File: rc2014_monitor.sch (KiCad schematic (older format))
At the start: 31 parts, among them J1 RC2014Pro, J3 USB_B_Micro, SW1 SW_Coded_Octal-8, U1 74HCT138, U2 74HCT151, U3 74HCT244, U4 74HCT244, U5 74HCT244, U6 74HCT32, U7 MAX40200AUK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

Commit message: added additional LED for 5V signal
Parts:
- removed RN1: R_Network06, Resistor_THT:R_Array_SIP7, symbol Device:R_Network06
- added LED6: SMD Red 620nm 40mcd 2.2V; 20mA, LED_SMD:LED_0805_2012Metric_Pad1.15x1.40mm_HandSolder, symbol Device:LED_Small
- added RN1: 270R Bussed, Resistor_THT:R_Array_SIP9, symbol Device:R_Network08
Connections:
- wire segments 151 -> 158
- no-connect marks 28 -> 26
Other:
- note added: "5V"
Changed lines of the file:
@@
-$EndComp
-$Comp
-L Device:R_Network06 RN1
-U 1 1 5CBFD2C7
-P 4850 3850
-F 0 "RN1" V 4333 3850 50  0000 C CNN
-F 1 "R_Network06" V 4424 3850 50  0000 C CNN
-F 2 "Resistor_THT:R_Array_SIP7" V 5225 3850 50  0001 C CNN
-F 3 "https://www.mouser.com/datasheet/2/54/600x-776645.pdf" H 4850 3850 50  0001 C CNN
-F 4 "652-4607X-1LF-270" V 4850 3850 50  0001 C CNN "MouserPN"
-F 5 "Bourns" H -500 50  50  0001 C CNN "MFR"
-F 6 "4607X-101-271LF" H -500 50  50  0001 C CNN "MPN"
-F 7 "Mouser" H -500 50  50  0001 C CNN "SPR"
-F 8 "652-4607X-1LF-270" H -500 50  50  0001 C CNN "SPN"
-F 9 "-" H -500 50  50  0001 C CNN "SPURL"
-	1    4850 3850
-	0    1    1    0
 $EndComp
 $Comp
@@
 NoConn ~ 1000 7000
 NoConn ~ 1000 7100
-NoConn ~ 4000 4250
-NoConn ~ 4000 4150
-NoConn ~ 4000 4050
 NoConn ~ 2550 1650
 NoConn ~ 2550 1750
@@
 NoConn ~ 10350 1650
 NoConn ~ 10350 1750
-NoConn ~ 4650 4050
 NoConn ~ 1000 6700
 NoConn ~ 1000 6800
@@
 Wire Wire Line
 	5550 6850 5750 6850
+$Comp
+L Device:R_Network08 RN1
+U 1 1 5CAEF515
+P 4850 3950
+F 0 "RN1" V 4233 3950 50  0000 C CNN
+F 1 "270R Bussed" V 4324 3950 50  0000 C CNN
+F 2 "Resistor_THT:R_Array_SIP9" V 5325 3950 50  0001 C CNN
+F 3 "https://www.mouser.com/datasheet/2/54/600x-776645.pdf" H 4850 3950 50  0001 C CNN
+F 4 "Bourns" V 4850 3950 50  0001 C CNN "MFR"
+F 5 "4609X-101-271LF" V 4850 3950 50  0001 C CNN "MPN"
+F 6 "Mouser" V 4850 3950 50  0001 C CNN "SPR"
+F 7 "652-4609X-1LF-270" V 4850 3950 50  0001 C CNN "SPN"
+F 8 "https://www.mouser.com/ProductDetail/652-4609X-1LF-270" V 4850 3950 50  0001 C CNN "SPURL"
+	1    4850 3950
+	0    1    1    0
+$EndComp
+NoConn ~ 4650 4150
+NoConn ~ 4650 4250
+$Comp
+L Device:LED_Small LED6
+U 1 1 5CB2ECC4
+P 4350 4050
+AR Path="/5CB2ECC4" Ref="LED6"  Part="1"
+AR Path="/5CB63856/5CB2ECC4" Ref="LED?"  Part="1"
+AR Path="/5CB5AB00/5CB63856/5CB2ECC4" Ref="LED?"  Part="1"
+F 0 "LED6" H 4500 4100 50  0000 C CNN
+F 1 "SMD Red 620nm 40mcd 2.2V; 20mA" H 4250 4100 50  0001 C CNN
+F 2 "LED_SMD:LED_0805_2012Metric_Pad1.15x1.40mm_HandSolder" V 4350 4050 50  0001 C CNN
+F 3 "https://www.mouser.com/datasheet/2/348/sml-h1(c)-e-1508182.pdf" V 4350 4050 50  0001 C CNN
+F 4 "755-SML-H12U8TT86C" H -500 150 50  0001 C CNN "MouserPN"
+F 5 "ROHM Semiconductor" H -500 150 50  0001 C CNN "MFR"
+F 6 "SML-H12U8TT86C" H -500 150 50  0001 C CNN "MPN"
+F 7 "Mouser" H -500 150 50  0001 C CNN "SPR"
+F 8 "755-SML-H12U8TT86C" H -500 150 50  0001 C CNN "SPN"
+F 9 "-" H -500 150 50  0001 C CNN "SPURL"
+	1    4350 4050
+	1    0    0    -1
+$EndComp
+Wire Wire Line
+	4450 4050 4650 4050
+Wire Wire Line
+	4250 4050 4050 4050
+Text Notes 4050 4050 0    50   ~ 0
+5V
+Wire Wire Line
+	4000 4150 4050 4150
+Wire Wire Line
+	4050 4150 4050 4050
+Connection ~ 4050 4050
+Wire Wire Line
+	4050 4050 4000 4050
+Wire Wire Line
+	4000 4250 4050 4250
+Wire Wire Line
+	4050 4250 4050 4150
+Connection ~ 4050 4150
 $EndSCHEMATC

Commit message: Added mounting hole
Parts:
- SW1: footprint Button_Switch_THT:Nidec_Copal_SH-7010C -> Button_Switch_THT:SW_Greyhill_94HBB08RAT_Octal_Angled
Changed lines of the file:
@@
 F 0 "SW1" H 2325 5317 50  0000 C CNN
 F 1 "SW_Coded_Octal-8" H 2325 5226 50  0000 C CNN
-F 2 "Button_Switch_THT:Nidec_Copal_SH-7010C" H 2275 4975 50  0001 C CNN
+F 2 "Button_Switch_THT:SW_Greyhill_94HBB08RAT_Octal_Angled" H 2275 4975 50  0001 C CNN
 F 3 "https://www.mouser.com/datasheet/2/626/DIP_Series_94H-334494.pdf" H 2275 4975 50  0001 C CNN
 F 4 "706-94HBB08RAT" H 2450 4450 50  0001 C CNN "Mouser PN"

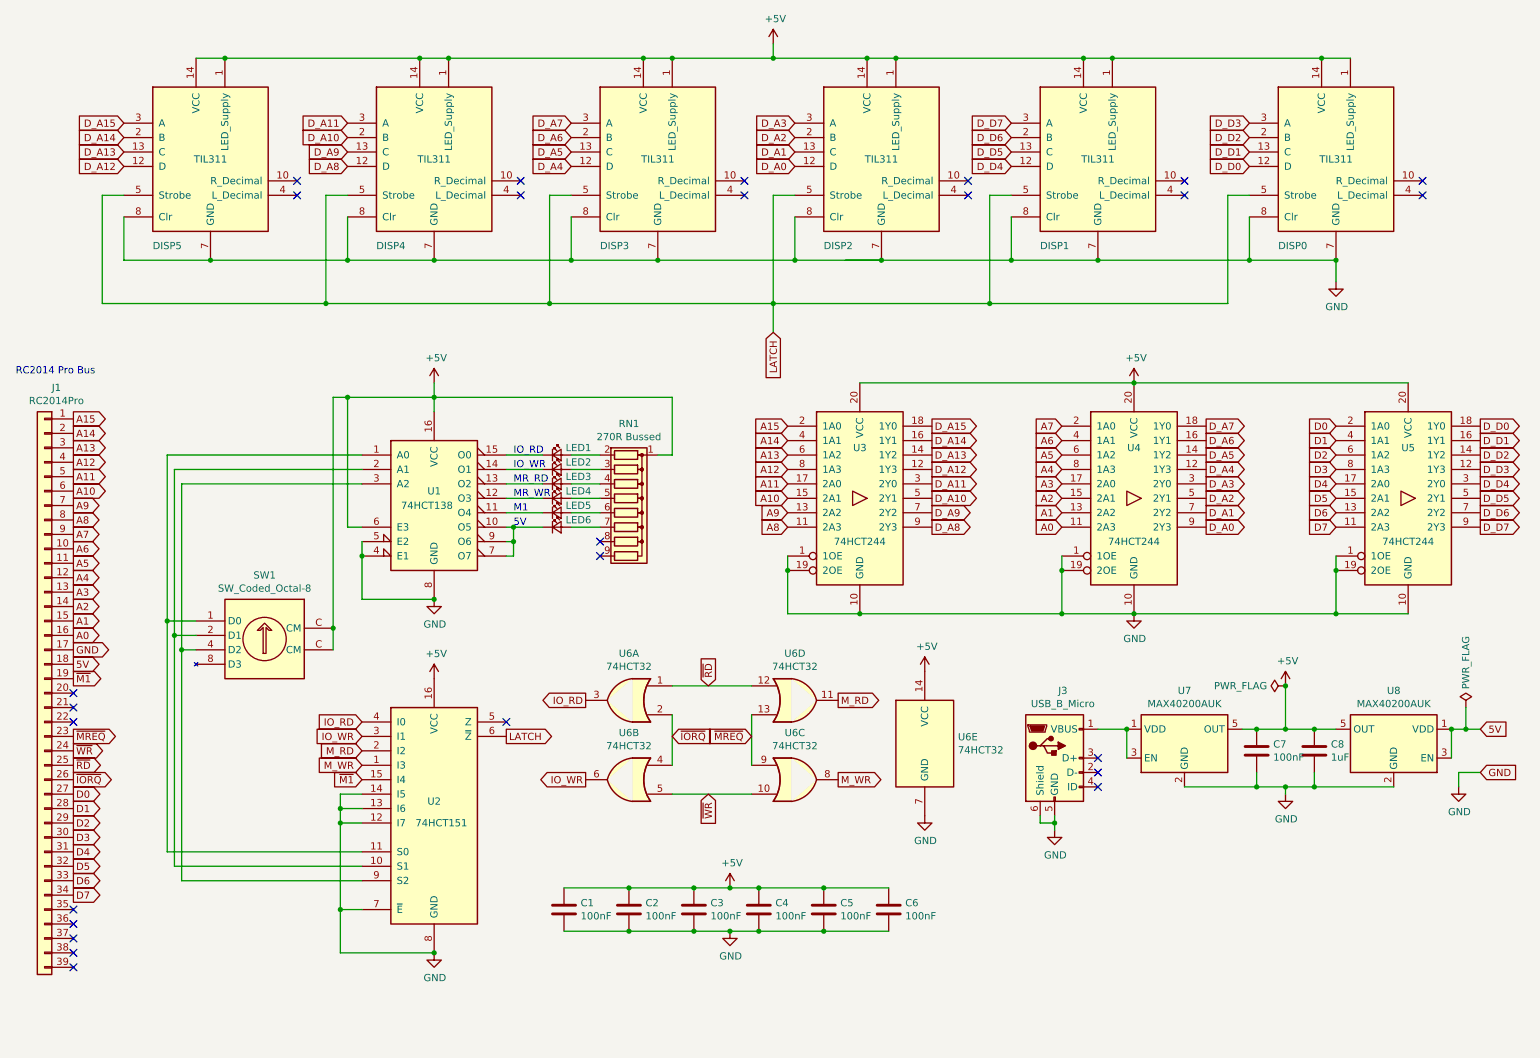
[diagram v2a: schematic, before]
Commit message: moved latch circuit to new sheet
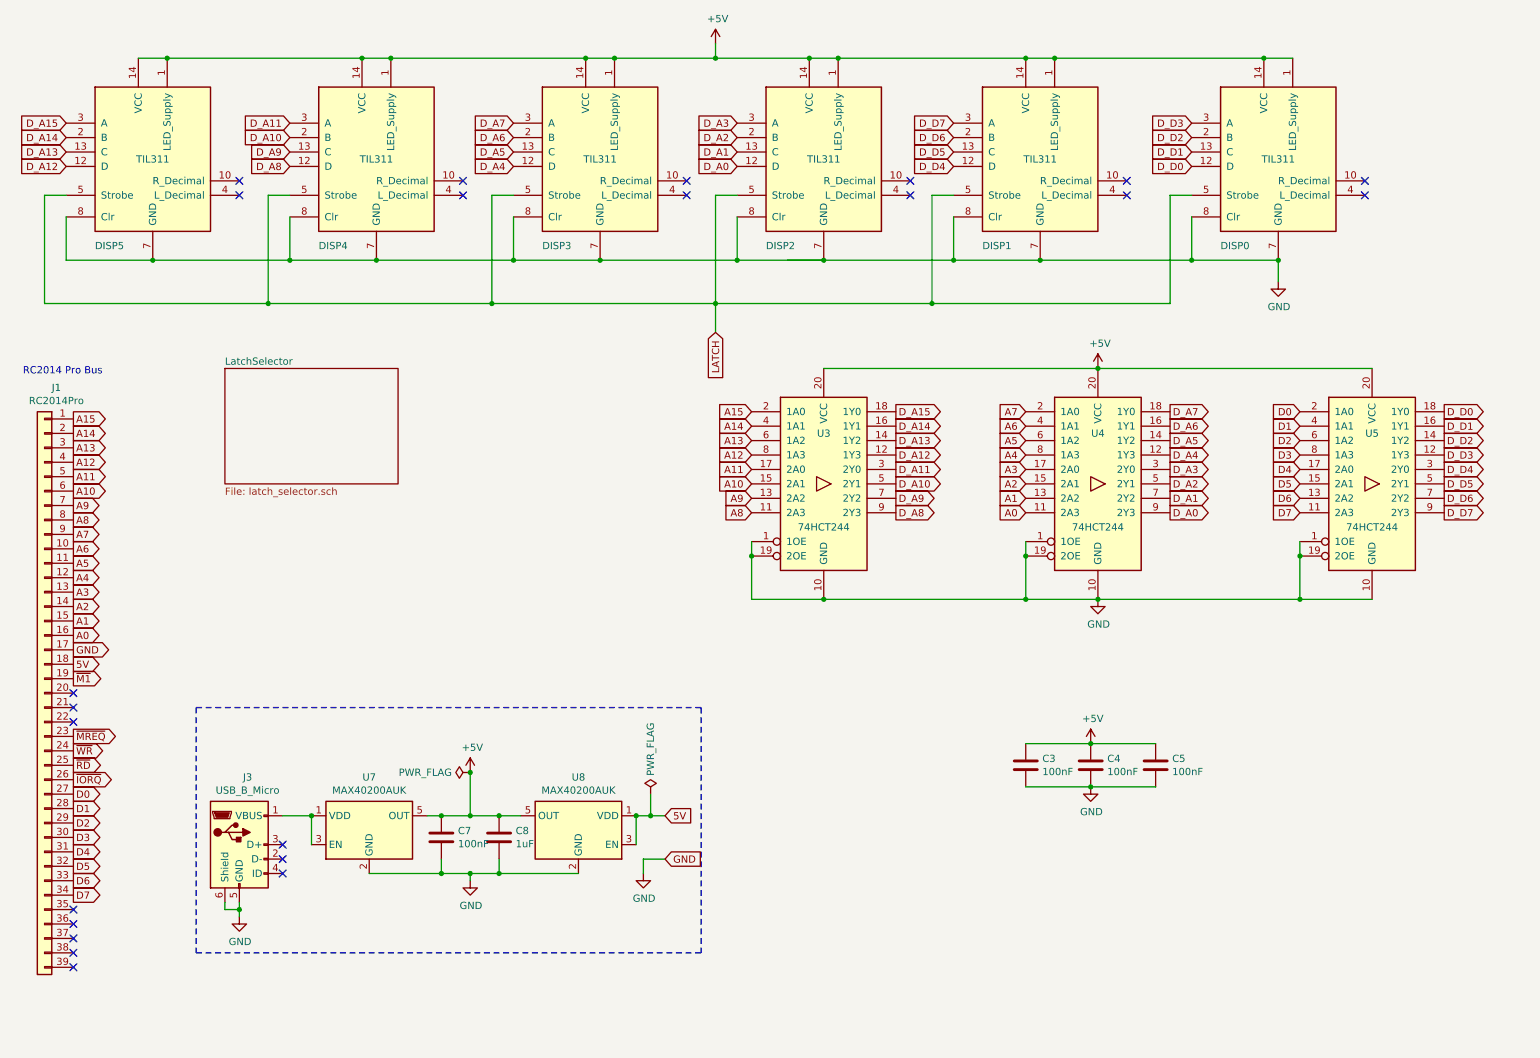
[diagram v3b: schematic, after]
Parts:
- removed C1, C2, C6: 100nF, Capacitor_THT:C_Disc_D5.0mm_W2.5mm_P2.50mm, symbol Device:C
- removed LED1, LED2, LED3, LED4, LED5, LED6: SMD Red 620nm 40mcd 2.2V; 20mA, LED_SMD:LED_0805_2012Metric_Pad1.15x1.40mm_HandSolder, symbol Device:LED_Small
- removed RN1: 270R Bussed, Resistor_THT:R_Array_SIP9, symbol Device:R_Network08
- removed SW1: SW_Coded_Octal-8, Button_Switch_THT:SW_Greyhill_94HBB08RAT_Octal_Angled, symbol rc2014_monitor-rescue:SW_Coded_Octal-8-Switch
- removed U1: 74HCT138, Package_DIP:DIP-16_W7.62mm, symbol rc2014_monitor-rescue:74HCT138-74xx
- removed U2: 74HCT151, Package_DIP:DIP-16_W7.62mm, symbol rc2014_monitor-rescue:74HCT151-74xx
- removed U6: 74HCT32, Package_DIP:DIP-14_W7.62mm, symbol rc2014_monitor-rescue:74HCT32-74xx
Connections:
- no-connect marks 26 -> 23
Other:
- note removed: "5V"
- note removed: "IO_RD\n"
- note removed: "IO_WR"
- note removed: "M1"
- note removed: "MR_RD"
- note removed: "MR_WR"
- moved on the sheet: C3, C4, C5, C7, C8, DISP0, DISP1, DISP2, DISP3, DISP4, DISP5, J3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

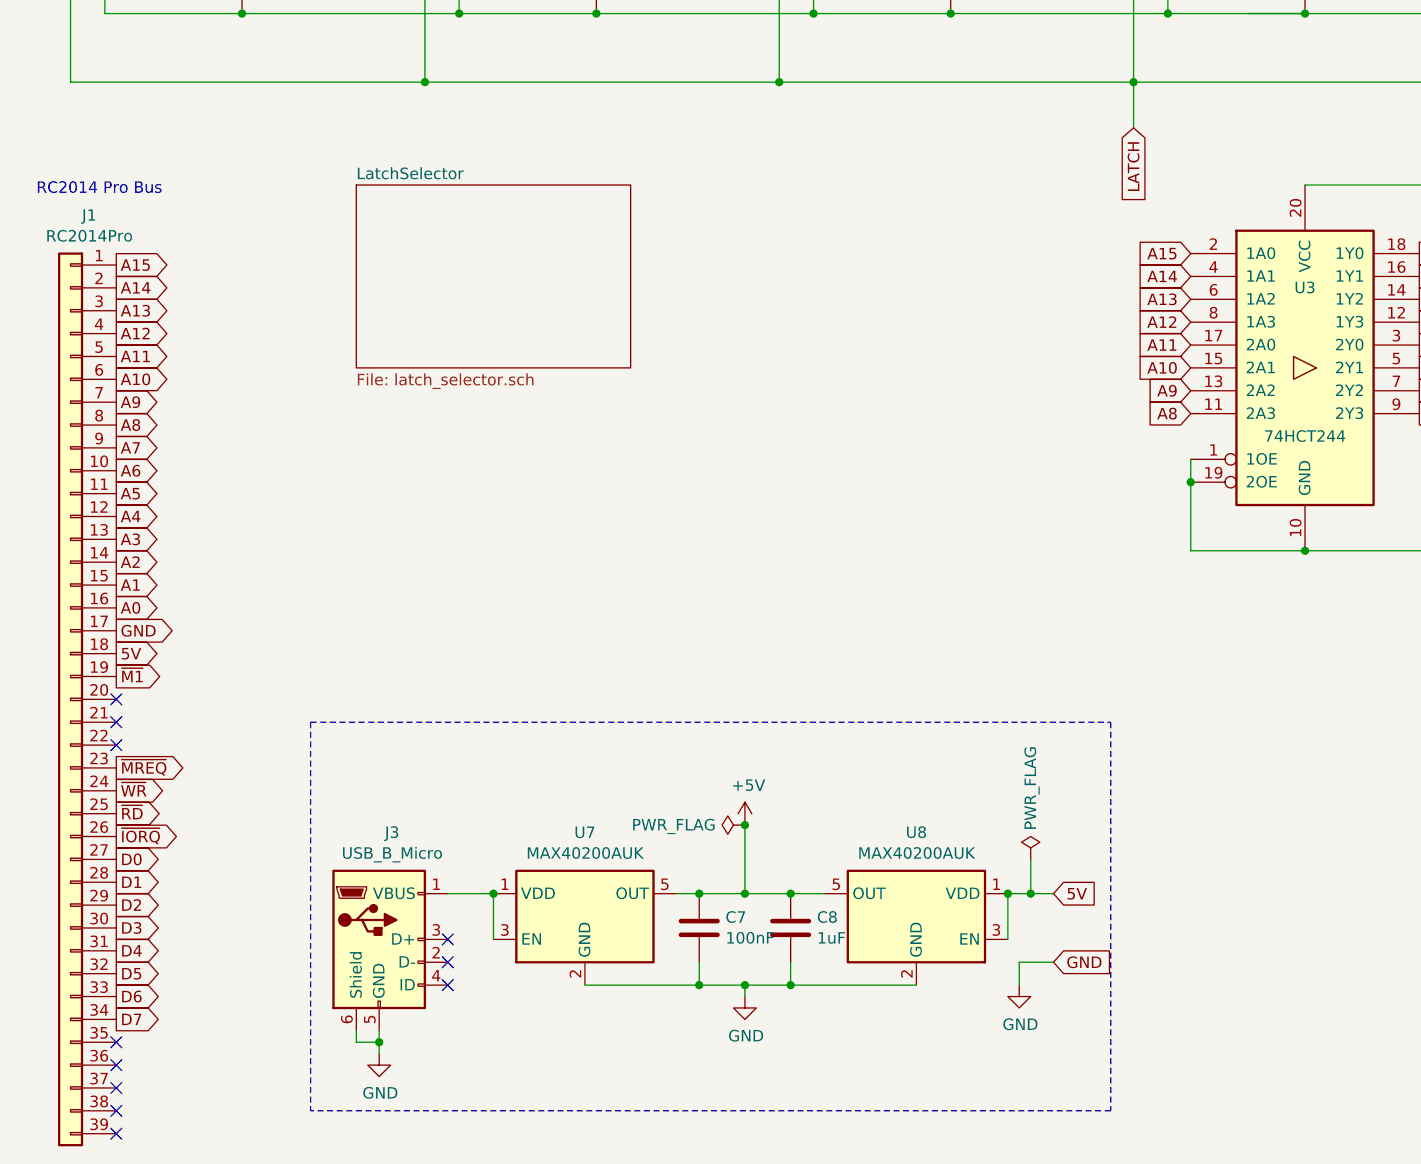
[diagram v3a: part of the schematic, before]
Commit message: added pro bus, generated gerbers
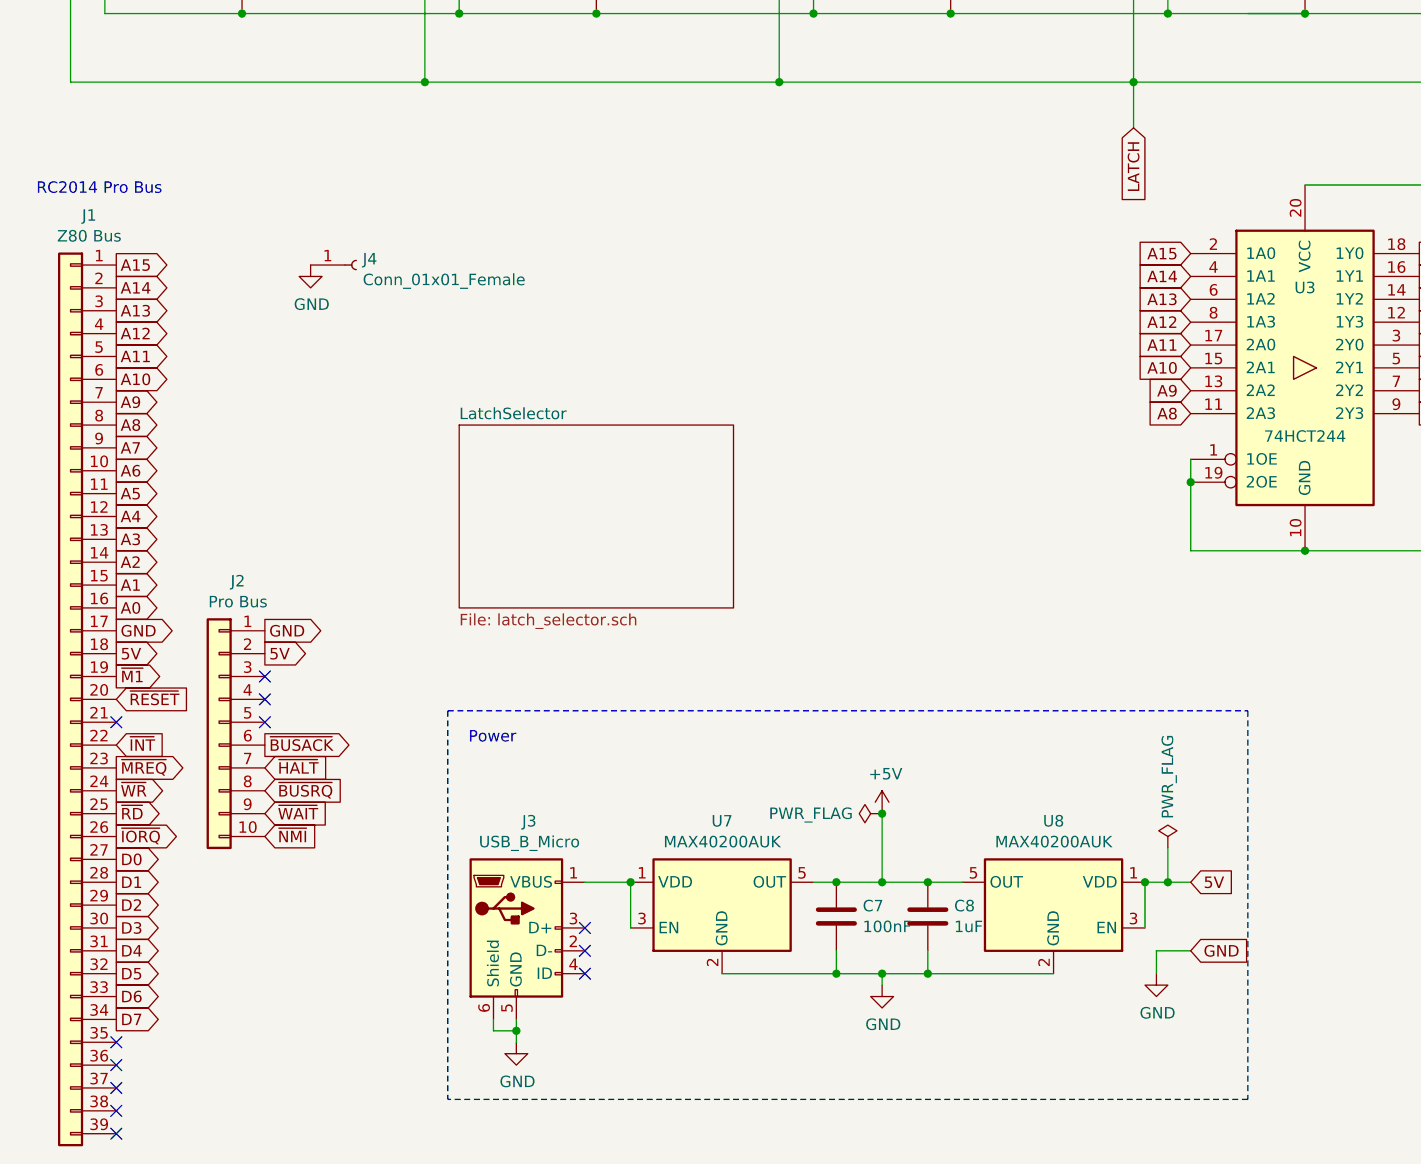
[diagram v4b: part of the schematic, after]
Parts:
- added J2: Pro Bus, Connector_PinHeader_2.54mm:PinHeader_1x10_P2.54mm_Vertical, symbol Connector_Generic:Conn_01x10
- added J4: Conn_01x01_Female, MountingHole:MountingHole_3.2mm_M3_ISO14580_Pad, symbol Connector:Conn_01x01_Female
- J1: value RC2014Pro -> Z80 Bus
- U7, U8: MFR (none) -> Maxim Integrated; MPN (none) -> MAX40200AUK+T; Mouser PN (none) -> 700-MAX40200AUK+T; SPN (none) -> 700-MAX40200AUK+T; SPR (none) -> Mouser; SPURL (none) -> https://www.mouser.com/ProductDetail/Maxim-Integrated/MAX40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
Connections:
- net 5V: now also J2.2 (Pin_2)
- net GND: now also J2.1 (Pin_1), J4.1 (Pin_1)
- net ~RESET: now reaches J1.20 (Pin_20)
- net ~INT: now reaches J1.22 (Pin_22)
- new net ~BUSACK: J2.6 (Pin_6)
- new net ~BUSRQ: J2.8 (Pin_8)
- new net ~HALT: J2.7 (Pin_7)
- new net ~NMI: J2.10 (Pin_10)
- new net ~WAIT: J2.9 (Pin_9)
- no-connect marks 23 -> 24
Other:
- note added: "Power"
- moved on the sheet: C7, C8, J3, U7, U8
